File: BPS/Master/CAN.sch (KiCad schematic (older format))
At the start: 19 parts, among them J8 CAN_Out, U12 CDSOT23-T24CAN, U13 ADM3055E

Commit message: Creates fan brd interface schematics and updates symbols/footprints related to the leader board
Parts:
- C25: renamed from C33; value 10uF -> 10u
- C26: renamed from C34; value 0.1uF -> 0.1u
- C27: renamed from C35; value 0.1uF -> 0.1u
- C28: renamed from C36; value 0.01uF -> 0.01u
- C29: value 0.22uF -> 0.22u
- C30: value 10uF -> 10u
- C31: value 0.1uF -> 0.1u
- C32: value 0.01uF -> 0.01u
- J8: symbol BPSMaster-rescue:CANConnector-utsvt-connectors -> utsvt-connectors:CANConnector
- L2: renamed from L3; value 2kH -> 2k
- L3: renamed from L4; value 2kH -> 2k
- U10: renamed from U13; symbol BPSMaster-rescue:ADM3055E-utsvt-chips -> utsvt-chips:ADM3055E
- U11: renamed from U12; symbol BPSMaster-rescue:CDSOT23-T24CAN-utsvt-chips -> utsvt-chips:CDSOT23-T24CAN
- renumbered R43 to R26, R41 to R27, R42 to R28
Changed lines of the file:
@@
 $EndDescr
 $Comp
-L BPSMaster-rescue:CANConnector-utsvt-connectors J8
+L utsvt-connectors:CANConnector J8
 U 1 1 5C2B42F3
 P 9250 3800
@@
 $EndComp
 $Comp
-L Device:R R42
+L Device:R R28
 U 1 1 5C2B42FA
 P 8200 3550
-F 0 "R42" V 8280 3550 50  0000 C CNN
+F 0 "R28" V 8280 3550 50  0000 C CNN
 F 1 "60" V 8200 3550 50  0000 C CNN
 F 2 "Resistor_SMD:R_0805_2012Metric" V 8130 3550 50  0001 C CNN
@@
 $EndComp
 $Comp
-L Device:R R41
+L Device:R R27
 U 1 1 5C2B4301
 P 8000 3550
-F 0 "R41" V 8080 3550 50  0000 C CNN
+F 0 "R27" V 8080 3550 50  0000 C CNN
 F 1 "60" V 8000 3550 50  0000 C CNN
 F 2 "Resistor_SMD:R_0805_2012Metric" V 7930 3550 50  0001 C CNN
@@
 $EndComp
 $Comp
-L Device:C_Small C33
+L Device:C_Small C25
 U 1 1 5C2B4310
 P 2150 3350
-F 0 "C33" H 2160 3420 50  0000 L CNN
-F 1 "10uF" H 2160 3270 50  0000 L CNN
+F 0 "C25" H 2160 3420 50  0000 L CNN
+F 1 "10u" H 2160 3270 50  0000 L CNN
 F 2 "Capacitor_SMD:C_0805_2012Metric" H 2150 3350 50  0001 C CNN
 F 3 "" H 2150 3350 50  0001 C CNN
@@
 $EndComp
 $Comp
-L Device:C_Small C34
+L Device:C_Small C26
 U 1 1 5C2B4317
 P 2500 3350
-F 0 "C34" H 2510 3420 50  0000 L CNN
-F 1 "0.1uF" H 2510 3270 50  0000 L CNN
+F 0 "C26" H 2510 3420 50  0000 L CNN
+F 1 "0.1u" H 2510 3270 50  0000 L CNN
 F 2 "Capacitor_SMD:C_0805_2012Metric" H 2500 3350 50  0001 C CNN
 F 3 "" H 2500 3350 50  0001 C CNN
@@
 $EndComp
 $Comp
-L Device:C_Small C35
+L Device:C_Small C27
 U 1 1 5C2B431E
 P 2950 3350
-F 0 "C35" H 2960 3420 50  0000 L CNN
-F 1 "0.1uF" H 2960 3270 50  0000 L CNN
+F 0 "C27" H 2960 3420 50  0000 L CNN
+F 1 "0.1u" H 2960 3270 50  0000 L CNN
 F 2 "Capacitor_SMD:C_0805_2012Metric" H 2950 3350 50  0001 C CNN
 F 3 "" H 2950 3350 50  0001 C CNN
@@
 $EndComp
 $Comp
-L Device:C_Small C36
+L Device:C_Small C28
 U 1 1 5C2B4325
 P 3300 3350
-F 0 "C36" H 3310 3420 50  0000 L CNN
-F 1 "0.01uF" H 3310 3270 50  0000 L CNN
+F 0 "C28" H 3310 3420 50  0000 L CNN
+F 1 "0.01u" H 3310 3270 50  0000 L CNN
 F 2 "Capacitor_SMD:C_0805_2012Metric" H 3300 3350 50  0001 C CNN
 F 3 "" H 3300 3350 50  0001 C CNN
@@
 P 6150 3200
 F 0 "C30" H 6160 3270 50  0000 L CNN
-F 1 "10uF" H 6160 3120 50  0000 L CNN
+F 1 "10u" H 6160 3120 50  0000 L CNN
 F 2 "Capacitor_SMD:C_0805_2012Metric" H 6150 3200 50  0001 C CNN
 F 3 "" H 6150 3200 50  0001 C CNN
@@
 P 5750 3200
 F 0 "C29" H 5760 3270 50  0000 L CNN
-F 1 "0.22uF" H 5760 3120 50  0000 L CNN
+F 1 "0.22u" H 5760 3120 50  0000 L CNN
 F 2 "Capacitor_SMD:C_0805_2012Metric" H 5750 3200 50  0001 C CNN
 F 3 "" H 5750 3200 50  0001 C CNN
@@
 $EndComp
 $Comp
-L Device:Ferrite_Bead_Small L3
+L Device:Ferrite_Bead_Small L2
 U 1 1 5C2B433C
 P 5950 3050
-F 0 "L3" V 5850 3100 50  0000 L CNN
-F 1 "2kH" V 5850 2900 50  0000 L CNN
+F 0 "L2" V 5850 3100 50  0000 L CNN
+F 1 "2k" V 5850 2900 50  0000 L CNN
 F 2 "Inductor_SMD:L_0805_2012Metric" V 5880 3050 50  0001 C CNN
 F 3 "" H 5950 3050 50  0001 C CNN
@@
 $EndComp
 $Comp
-L Device:Ferrite_Bead_Small L4
+L Device:Ferrite_Bead_Small L3
 U 1 1 5C2B4343
 P 5950 3350
-F 0 "L4" V 6050 3400 50  0000 L CNN
-F 1 "2kH" V 6050 3200 50  0000 L CNN
+F 0 "L3" V 6050 3400 50  0000 L CNN
+F 1 "2k" V 6050 3200 50  0000 L CNN
 F 2 "Inductor_SMD:L_0805_2012Metric" V 5880 3350 50  0001 C CNN
 F 3 "" H 5950 3350 50  0001 C CNN
@@
 P 6550 3200
 F 0 "C31" H 6560 3270 50  0000 L CNN
-F 1 "0.1uF" H 6560 3120 50  0000 L CNN
+F 1 "0.1u" H 6560 3120 50  0000 L CNN
 F 2 "Capacitor_SMD:C_0805_2012Metric" H 6550 3200 50  0001 C CNN
 F 3 "" H 6550 3200 50  0001 C CNN
@@
 P 6850 3200
 F 0 "C32" H 6860 3270 50  0000 L CNN
-F 1 "0.01uF" H 6860 3120 50  0000 L CNN
+F 1 "0.01u" H 6860 3120 50  0000 L CNN
 F 2 "Capacitor_SMD:C_0805_2012Metric" H 6850 3200 50  0001 C CNN
 F 3 "" H 6850 3200 50  0001 C CNN
@@
 $EndComp
 $Comp
-L BPSMaster-rescue:ADM3055E-utsvt-chips U13
+L utsvt-chips:ADM3055E U10
 U 1 1 5C2B4359
 P 4350 3600
-F 0 "U13" H 4100 4250 60  0000 C CNN
+F 0 "U10" H 4100 4250 60  0000 C CNN
 F 1 "ADM3055E" H 4550 3500 60  0000 C CNN
 F 2 "UTSVT_ICs:SOIC-20W_7.5x15.4mm_Pitch1.27mm" H 4350 3700 60  0001 C CNN
@@
 NoConn ~ 3650 4100
 $Comp
-L power:PWR_FLAG #FLG04
+L power:PWR_FLAG #FLG03
 U 1 1 5C2B4394
 P 7300 3000
-F 0 "#FLG04" H 7300 3075 50  0001 C CNN
+F 0 "#FLG03" H 7300 3075 50  0001 C CNN
 F 1 "PWR_FLAG" H 7300 2900 30  0000 C CNN
 F 2 "" H 7300 3000 50  0001 C CNN
@@
 $EndComp
 $Comp
-L power:PWR_FLAG #FLG05
+L power:PWR_FLAG #FLG04
 U 1 1 5C2B439A
 P 7300 3200
-F 0 "#FLG05" H 7300 3275 50  0001 C CNN
+F 0 "#FLG04" H 7300 3275 50  0001 C CNN
 F 1 "PWR_FLAG" H 7200 3150 50  0001 L CNN
 F 2 "" H 7300 3200 50  0001 C CNN
@@
 $EndComp
 $Comp
-L BPSMaster-rescue:CDSOT23-T24CAN-utsvt-chips U12
+L utsvt-chips:CDSOT23-T24CAN U11
 U 1 1 5C2B43A0
 P 8100 2850
-F 0 "U12" H 8100 2700 60  0000 C CNN
+F 0 "U11" H 8100 2700 60  0000 C CNN
 F 1 "CDSOT23-T24CAN" H 8100 3000 60  0000 C CNN
 F 2 "Package_TO_SOT_SMD:SOT-23W" H 8100 2850 60  0001 C CNN
@@
 $EndComp
 $Comp
-L Device:R R43
+L Device:R R26
 U 1 1 5C2B43C4
 P 5550 4150
-F 0 "R43" V 5630 4150 50  0000 C CNN
+F 0 "R26" V 5630 4150 50  0000 C CNN
 F 1 "0" V 5550 4150 50  0000 C CNN
 F 2 "Resistor_SMD:R_0805_2012Metric" V 5480 4150 50  0001 C CNN
@@
 	5250 3050 5250 3150
 $Comp
-L power:GND #PWR071
+L power:GND #PWR060
 U 1 1 5C28BDDE
 P 2150 3550
-F 0 "#PWR071" H 2150 3300 50  0001 C CNN
+F 0 "#PWR060" H 2150 3300 50  0001 C CNN
 F 1 "GND" H 2300 3500 50  0000 C CNN
 F 2 "" H 2150 3550 50  0001 C CNN
@@
 	2500 3000 2500 3100
 $Comp
-L power:+3.3V #PWR070
+L power:+3.3V #PWR062
 U 1 1 5C4ABE05
 P 2950 3000
-F 0 "#PWR070" H 2950 2850 50  0001 C CNN
+F 0 "#PWR062" H 2950 2850 50  0001 C CNN
 F 1 "+3.3V" H 2965 3173 50  0000 C CNN
 F 2 "" H 2950 3000 50  0001 C CNN
@@
 	2950 3000 2950 3200
 $Comp
-L power:+5V #PWR069
+L power:+5V #PWR061
 U 1 1 5C4C2AB0
 P 2500 3000
-F 0 "#PWR069" H 2500 2850 50  0001 C CNN
+F 0 "#PWR061" H 2500 2850 50  0001 C CNN
 F 1 "+5V" H 2515 3173 50  0000 C CNN
 F 2 "" H 2500 3000 50  0001 C CNN

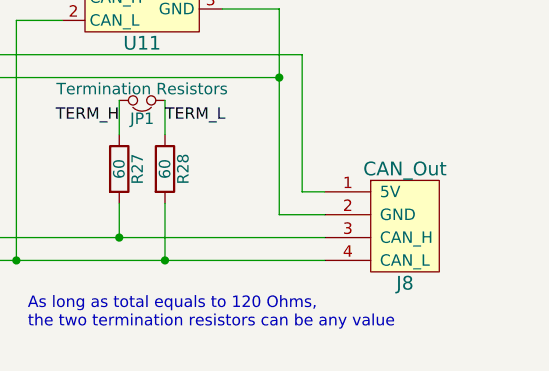
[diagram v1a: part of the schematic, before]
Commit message: Finishes schematics for bps leader board
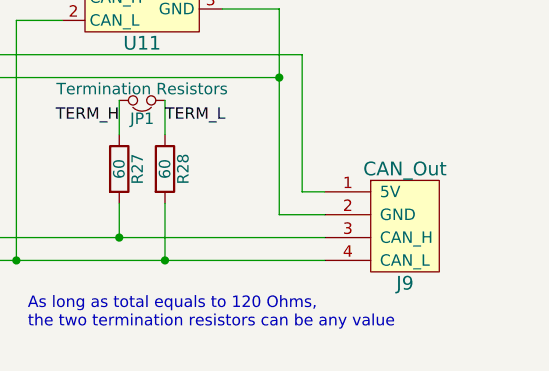
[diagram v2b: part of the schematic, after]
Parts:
- renumbered J8 to J9
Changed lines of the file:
@@
 $Descr A4 11693 8268
 encoding utf-8
-Sheet 7 10
+Sheet 7 11
 Title ""
 Date ""
@@
 $EndDescr
 $Comp
-L utsvt-connectors:CANConnector J8
+L utsvt-connectors:CANConnector J9
 U 1 1 5C2B42F3
 P 9250 3800
-F 0 "J8" H 9250 3550 60  0000 C CNN
+F 0 "J9" H 9250 3550 60  0000 C CNN
 F 1 "CAN_Out" H 9250 4050 60  0000 C CNN
 F 2 "UTSVT_Connectors:Molex_MicroFit3.0_1x4xP3.00mm_PolarizingPeg_Vertical" H 9400 4100 60  0001 C CNN
@@
 	5250 3050 5250 3150
 $Comp
-L power:GND #PWR060
+L power:GND #PWR063
 U 1 1 5C28BDDE
 P 2150 3550
-F 0 "#PWR060" H 2150 3300 50  0001 C CNN
+F 0 "#PWR063" H 2150 3300 50  0001 C CNN
 F 1 "GND" H 2300 3500 50  0000 C CNN
 F 2 "" H 2150 3550 50  0001 C CNN
@@
 	2500 3000 2500 3100
 $Comp
-L power:+3.3V #PWR062
+L power:+3.3V #PWR065
 U 1 1 5C4ABE05
 P 2950 3000
-F 0 "#PWR062" H 2950 2850 50  0001 C CNN
+F 0 "#PWR065" H 2950 2850 50  0001 C CNN
 F 1 "+3.3V" H 2965 3173 50  0000 C CNN
 F 2 "" H 2950 3000 50  0001 C CNN
@@
 	2950 3000 2950 3200
 $Comp
-L power:+5V #PWR061
+L power:+5V #PWR064
 U 1 1 5C4C2AB0
 P 2500 3000
-F 0 "#PWR061" H 2500 2850 50  0001 C CNN
+F 0 "#PWR064" H 2500 2850 50  0001 C CNN
 F 1 "+5V" H 2515 3173 50  0000 C CNN
 F 2 "" H 2500 3000 50  0001 C CNN
